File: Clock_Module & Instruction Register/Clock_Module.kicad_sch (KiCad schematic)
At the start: 1 part, among them J1 PC104

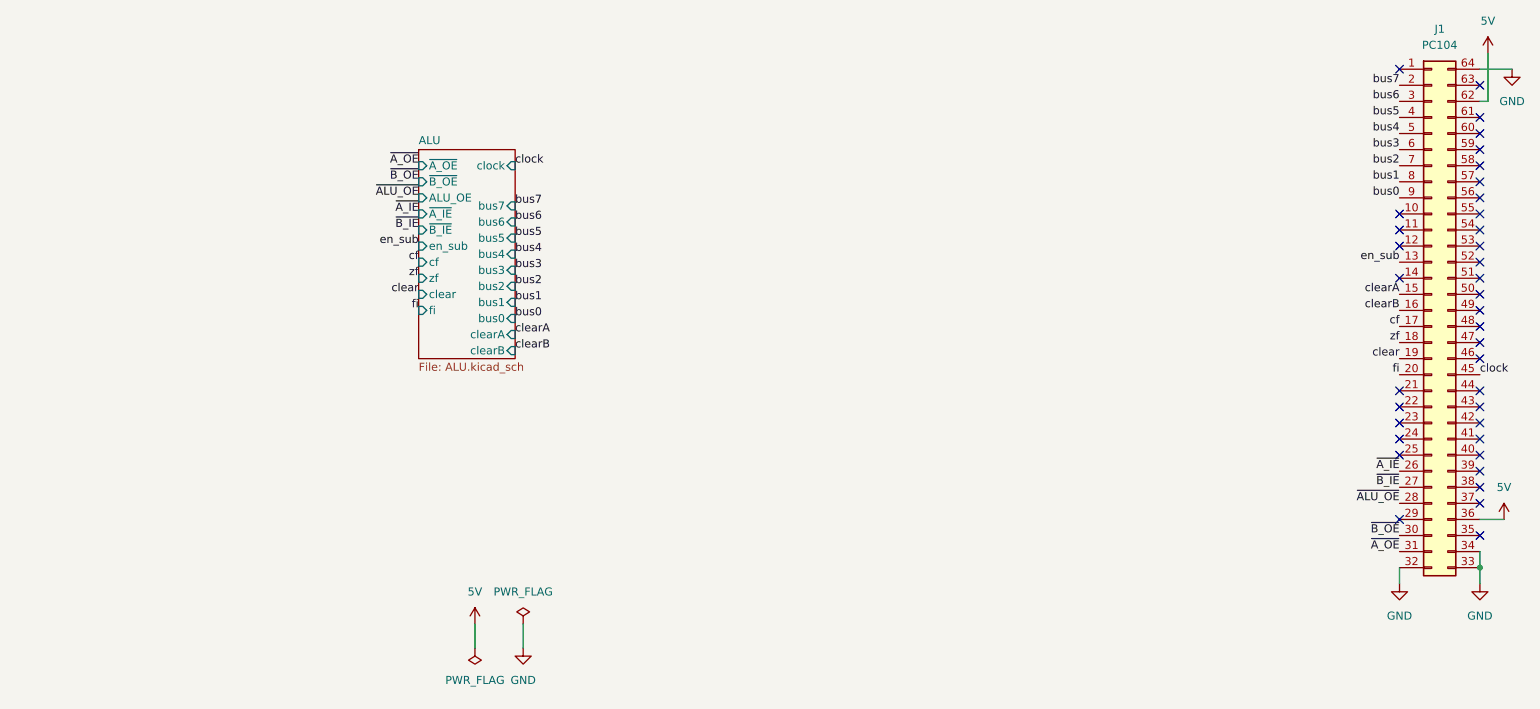
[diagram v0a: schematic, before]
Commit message: Placed clock module again
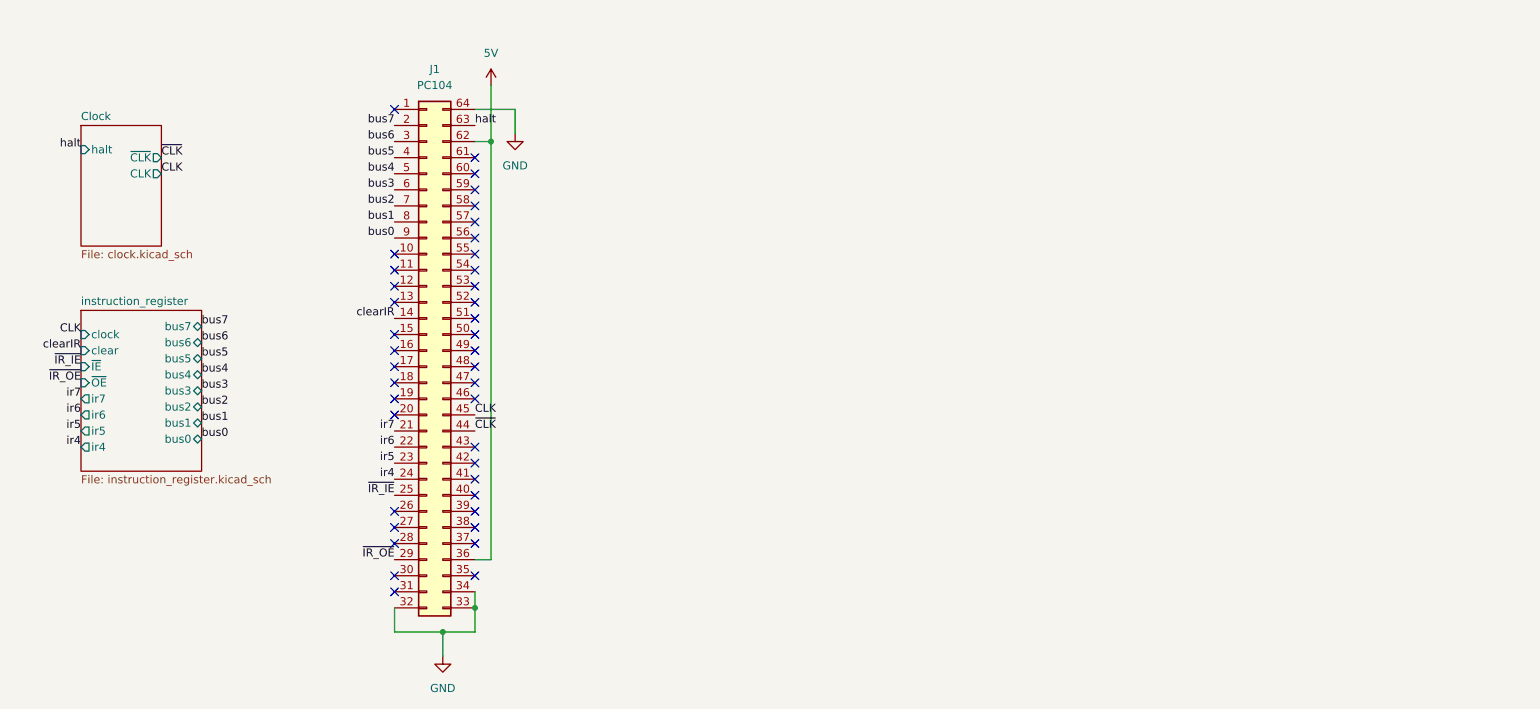
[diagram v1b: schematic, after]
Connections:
- net clearIR: now reaches J1.14 (Pin_14)
- net ir7: now reaches J1.21 (Pin_21)
- net ir6: now reaches J1.22 (Pin_22)
- net ir5: now reaches J1.23 (Pin_23)
- net ir4: now reaches J1.24 (Pin_24)
- net ~{IR_IE}: now reaches J1.25 (Pin_25)
- net ~{IR_OE}: now reaches J1.29 (Pin_29)
- net ~{CLK}: now reaches J1.44 (Pin_44)
- net halt: now reaches J1.63 (Pin_63)
- net cf: no longer names the net of J1.17 (Pin_17)
- net clear: no longer names the net of J1.19 (Pin_19)
- net clearA: no longer names the net of J1.15 (Pin_15)
- net clearB: no longer names the net of J1.16 (Pin_16)
- net clock renamed CLK
- net en_sub: no longer names the net of J1.13 (Pin_13)
- net fi: no longer names the net of J1.20 (Pin_20)
- net zf: no longer names the net of J1.18 (Pin_18)
- net ~{ALU_OE}: no longer names the net of J1.28 (Pin_28)
- net ~{A_IE}: no longer names the net of J1.26 (Pin_26)
- net ~{A_OE}: no longer names the net of J1.31 (Pin_31)
- net ~{B_IE}: no longer names the net of J1.27 (Pin_27)
- net ~{B_OE}: no longer names the net of J1.30 (Pin_30)
- no-connect marks 37 -> 40
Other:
- removed sheet ALU
- added sheet Clock (clock.kicad_sch)
- added sheet instruction_register (instruction_register.kicad_sch)
- title: Arithmethic Logic Unit -> Clock Module
